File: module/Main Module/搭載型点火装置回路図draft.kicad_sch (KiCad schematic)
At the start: 30 parts, among them Q1 NPN, Q2 BS250, Q3 BS170, SW1 SW_DPDT_x2

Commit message: Remerged
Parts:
- removed D2: D_Zener_Small_Filled, symbol Device:D_Zener_Small_Filled
- removed R6: R_US, symbol Device:R_US
- added D2: 1N914, Diode_THT:D_DO-35_SOD27_P7.62mm_Horizontal, symbol Diode:1N914
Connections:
- net Alart: now also D2.2 (A)
- net at FLIGHTPIN., IGNITER.: now also Q3.1 (D), SW1.3 (C); no longer SW1.1 (A)
- net at D1.1 (K), R5.2: now also D2.1 (K)
- new net: FLIGHTPIN., IGNITER., SW1.1 (A)
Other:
- moved on the sheet: BZ1, D3, R15

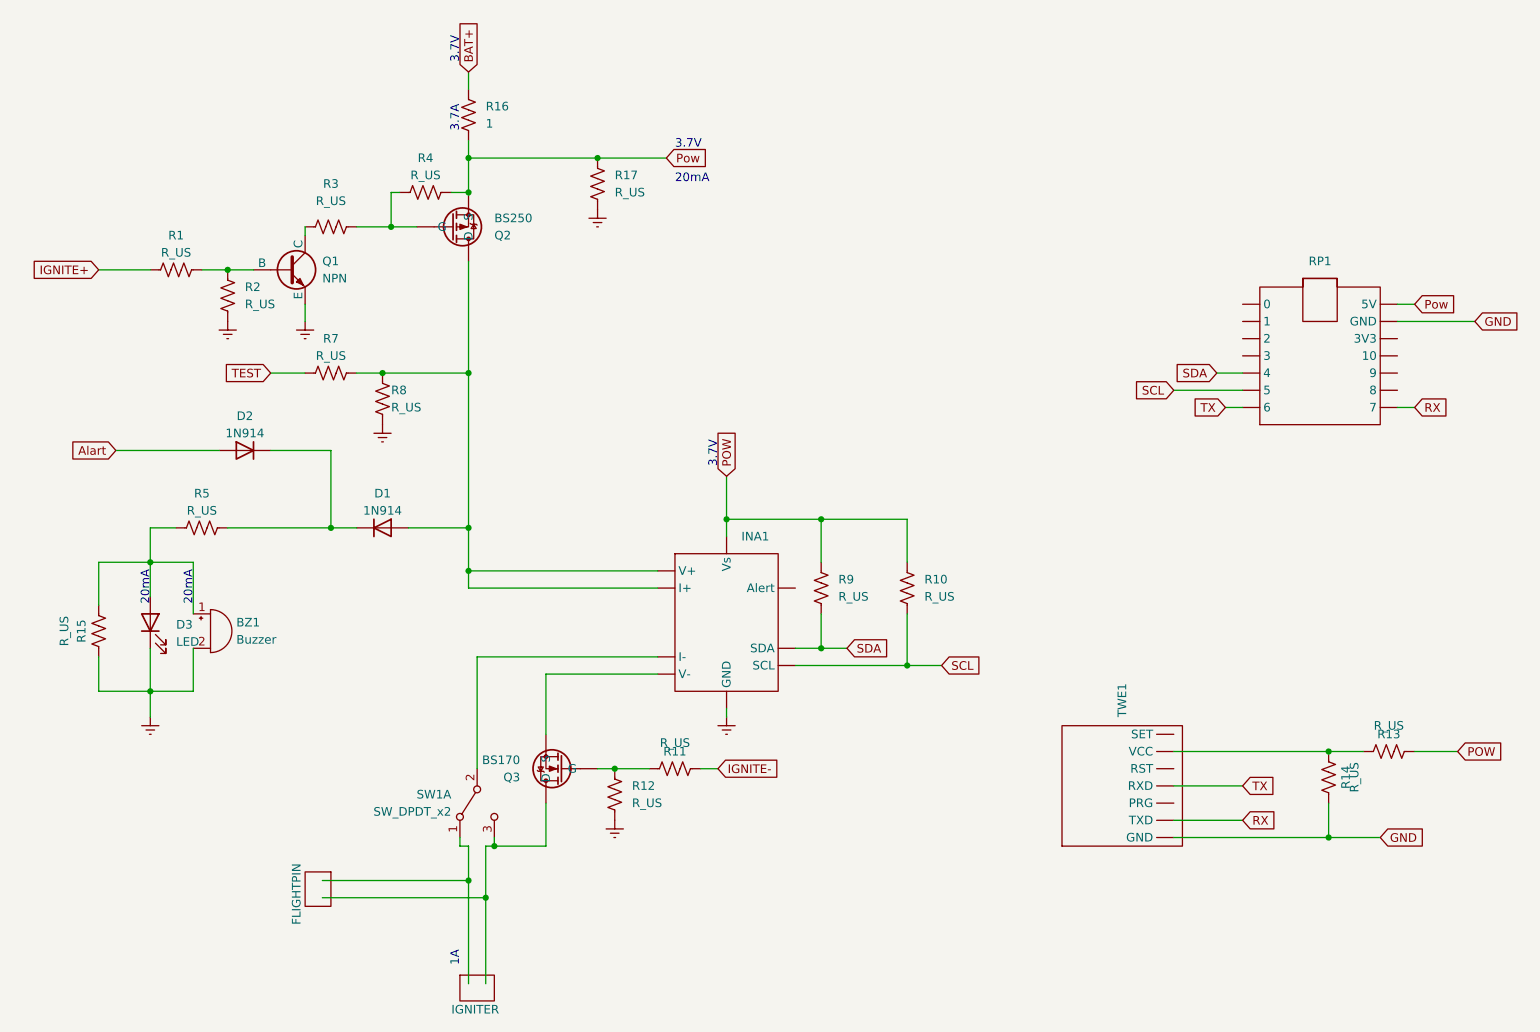
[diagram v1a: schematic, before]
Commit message: 抵抗値を一部計算しました
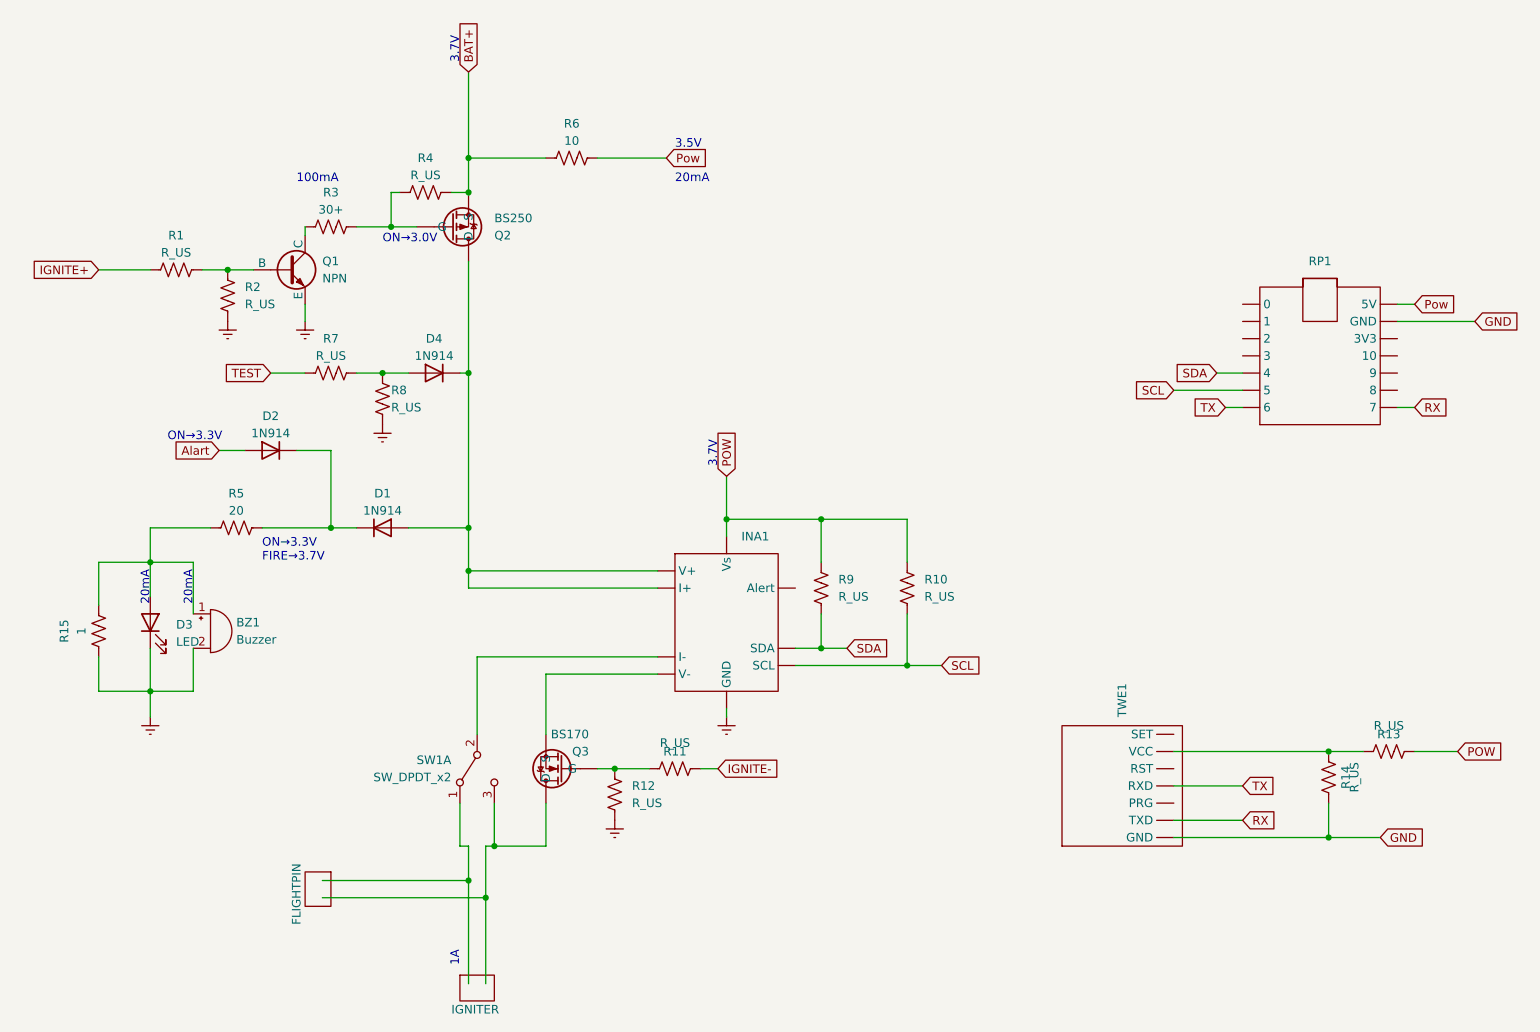
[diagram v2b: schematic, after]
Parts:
- removed R16: 1, symbol Device:R_US
- removed R17: R_US, symbol Device:R_US
- added D4: 1N914, Diode_THT:D_DO-35_SOD27_P7.62mm_Horizontal, symbol Diode:1N914
- added R6: 10, symbol Device:R_US
- R15: value R_US -> 1
- R3: value R_US -> 30+
- R5: value R_US -> 20
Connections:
- net BAT+: now also Q2.3 (S), R4.1, R6.2
- net Earth: now also R15.1; no longer R15.2
- net Pow: now also R6.1; no longer Q2.3 (S), R4.1
- net at BZ1.1 (-), D3.2 (A), R5.1: now also R15.2; no longer R15.1
- net at FLIGHTPIN., IGNITER.: now also Q3.1 (D), SW1.3 (C); no longer SW1.1 (A)
- new net: D4.2 (A), R7.1, R8.1
- new net: FLIGHTPIN., IGNITER., SW1.1 (A)
- new net: D1.2 (A), D4.1 (K), INA1. (Vs), Q2.1 (D)
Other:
- note added: "100mA"
- note added: "3.5V"
- note added: "ON→3.0V"
- note added: "ON→3.3V"
- note added: "ON→3.3V FIRE→3.7V"
- note removed: "3.7A"
- moved on the sheet: D2, R15, R5, SW1A
